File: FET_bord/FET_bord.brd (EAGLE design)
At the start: 100 x 80 mm, 4 parts

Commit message: スナバ回路資料追加
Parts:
- added CPOL1, CPOL2, CPOL3: C_DEKAI, user_rcl:1014CAPA
- added R1: 0, user_rcl:1608
- added R_I1, R_I2: (no value), user_rcl:0603X4RESISTOR
- added U$1: VL_4P, user_conector:VL_4P
- added U$2: A3921, user_ic:TSSOP_28P_ALLEGRO
- added U$3: ACS711, user_ic:SOIC8
- added U$4: HS38382, user_heatshink:38X38SQ
- added U$5, U$7: FDC6305, user_tr_fet_igbt:SSOT6
- added U$6: RGB_LED, user_leds:RGB_LED
- added U$8: TLP290-4, user_ic:TLP290
- moved TR2 81.3 mm to (47.0, 31.8), turned to 270 degrees
- moved TR1 66.1 mm to (47.0, 7.62), turned to 270 degrees
- moved TR4 53.3 mm to (21.6, 31.8), turned to 270 degrees
- moved TR3 47.3 mm to (21.6, 7.62), turned to 270 degrees
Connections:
- new net FF1: U$5.1, U$7.1
- new net FF2: U$5.3, U$7.3
- new net GHA: U$2.PIN10
- new net GHB: U$2.PIN5
- new net GLA: U$2.PIN12
- new net GLB: U$2.PIN3
- new net GND: CPOL1.-, CPOL2.-, CPOL3.-, R1.2, TR3.3, TR4.3, U$1.P$4
- new net GNDI: R1.1, U$2.PAD, U$2.PIN17, U$5.2, U$5.5, U$6.B_A
- new net M: U$1.P$3, U$3.P$1, U$3.P$2
- new net N$1: U$5.6, U$6.R_A
- new net N$2: TR1.3, TR3.2, U$3.P$3, U$3.P$4
- new net N$3: TR2.3, TR4.2
- new net N$4: U$1.P$2
- new net N$5: U$5.4, U$6.G_A
- new net N$6: R_I1.1, U$6.R_K
- new net N$7: R_I1.2, U$6.G_K
- new net N$8: R_I1.3, U$6.B_K
- new net SA: U$2.PIN11
- new net SB: U$2.PIN4
- new net VDD: CPOL1.+, CPOL2.+, CPOL3.+, TR1.2, TR2.2, U$1.P$1
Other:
- board size 100 x 80 mm -> 85 x 54 mm

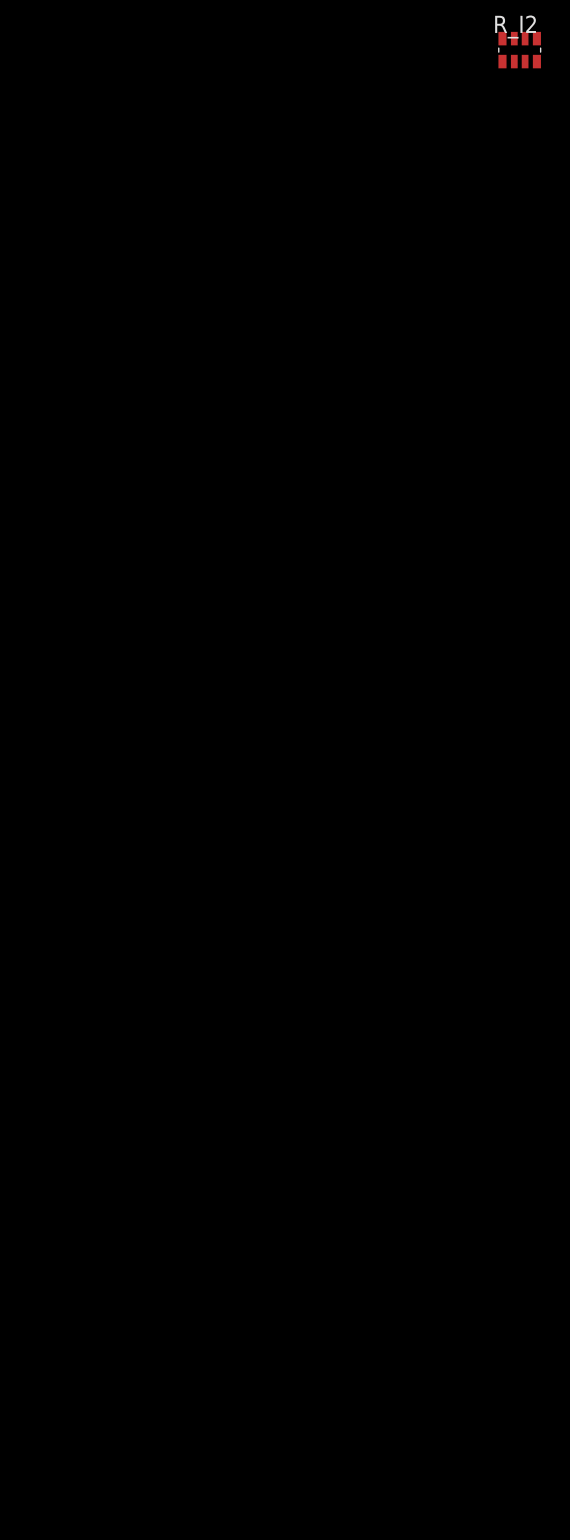
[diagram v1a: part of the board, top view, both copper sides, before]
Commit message: スナバ追加
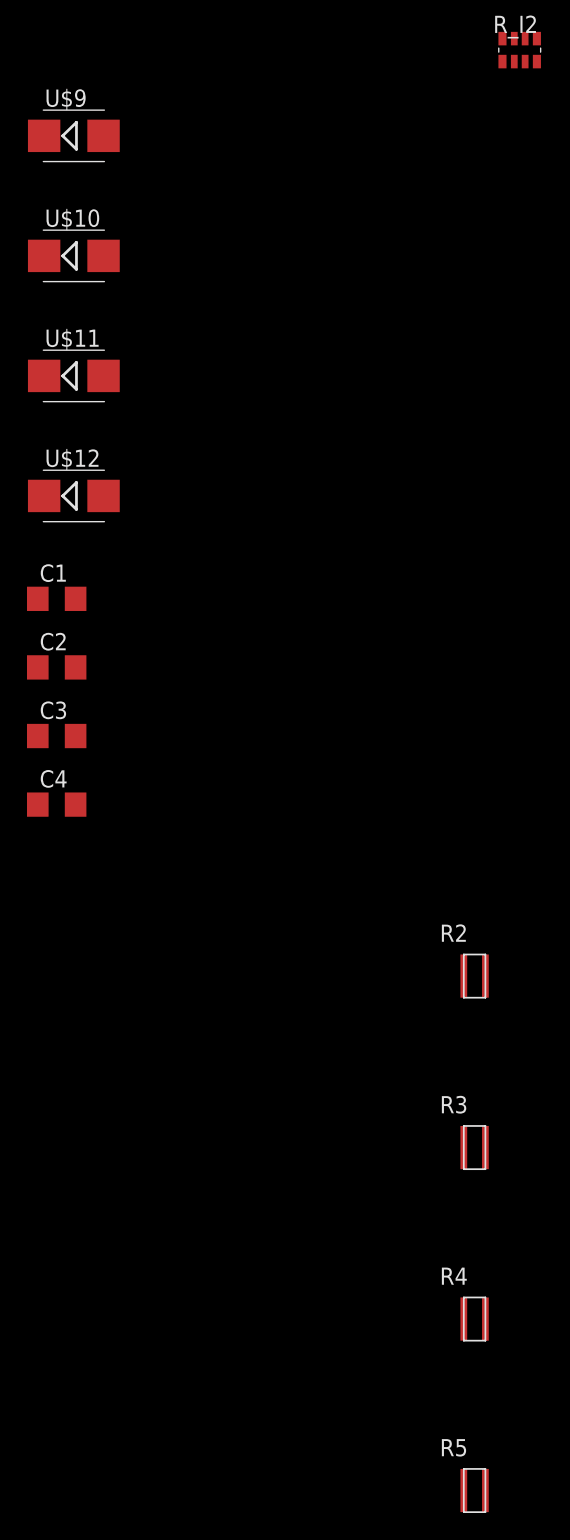
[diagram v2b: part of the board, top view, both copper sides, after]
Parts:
- added C1, C2, C3, C4: 0.1u, rcl:C3216
- added R2, R3, R4, R5: (no value), user_rcl:1632
- added U$10, U$11, U$12, U$9: ES3BB13F, user_diode:SMB
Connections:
- new net N$10: C2.2, R3.P$2, U$9.A
- new net N$11: C3.2, R4.P$2, U$12.A
- new net N$12: C4.1, R5.P$1, U$11.C
- new net N$9: C1.1, R2.P$1, U$10.C
- net GND: now also C1.2, C4.2, R3.P$1, R4.P$1
- net N$2: now also U$10.A, U$9.C
- net N$3: now also U$11.A, U$12.C
- net VDD: now also C2.1, C3.1, R2.P$2, R5.P$2

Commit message: a3921ロジック回路周りの設計
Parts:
- added C5: 0.1u, rcl:C1608
- added R6: (no value), user_rcl:1608
- added R7: 20k, user_rcl:1608
- added R_I3, R_I4: 10k, user_rcl:1005X4RESISTOR
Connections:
- new net N$13: R_I3.1, U$2.PIN23
- new net N$14: R_I3.2, U$2.PIN22
- new net N$15: R_I3.3, U$2.PIN21
- new net N$16: R_I3.4, U$2.PIN19
- new net RDEAD: U$2.PIN27
- new net RESET: U$2.PIN24
- new net V5: C5.1, R_I3.5, R_I3.6, R_I3.7, R_I4.5, R_I4.6, R_I4.7, U$2.PIN20
- new net VDSTH: R6.1, R7.1, R_I4.1, R_I4.4, U$2.PIN28
- net FF1: now also R_I4.2, U$2.PIN25
- net FF2: now also R_I4.3, U$2.PIN26
- net GNDI: now also C5.2, R6.2, R7.2, R_I3.8, R_I4.8
- net VDD: now also U$2.PIN13
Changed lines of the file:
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@@
 <attribute name="VALUE" x="-33.02" y="-105.41" size="1.27" layer="27"/>
+</element>
+<element name="R_I3" library="user_rcl" package="1005X4RESISTOR" value="10k" x="-33.02" y="-157.48" smashed="yes"/>
+<element name="R_I4" library="user_rcl" package="1005X4RESISTOR" value="10k" x="-33.02" y="-160.02" smashed="yes"/>
+<element name="C5" library="rcl" library_urn="urn:adsk.eagle:library:334" package="C1608" package3d_urn="urn:adsk.eagle:package:23621/2" value="0.1u" x="-31.75" y="-163.83" smashed="yes">
+<attribute name="NAME" x="-32.385" y="-163.195" size="1.27" layer="25"/>
+<attribute name="POPULARITY" value="3" x="-31.75" y="-163.83" size="1.778" layer="27" display="off"/>
+<attribute name="SPICEPREFIX" value="C" x="-31.75" y="-163.83" size="1.778" layer="27" display="off"/>
+<attribute name="VALUE" x="-32.385" y="-165.735" size="1.27" layer="27"/>
+</element>
+<element name="R6" library="user_rcl" package="1608" value="" x="-31.75" y="-168.91" smashed="yes">
+<attribute name="NAME" x="-32.385" y="-168.275" size="1.27" layer="25"/>
+<attribute name="VALUE" x="-32.385" y="-170.815" size="1.27" layer="27"/>
+</element>
+<element name="R7" library="user_rcl" package="1608" value="20k" x="-31.75" y="-172.72" smashed="yes">
+<attribute name="NAME" x="-32.385" y="-172.085" size="1.27" layer="25"/>
+<attribute name="VALUE" x="-32.385" y="-174.625" size="1.27" layer="27"/>
 </element>
 </elements>
@@
 <contactref element="R2" pad="P$2"/>
 <contactref element="R5" pad="P$2"/>
+<contactref element="U$2" pad="PIN13"/>
 <wire x1="0" y1="-115.57" x2="0" y2="-153.67" width="0" layer="19" extent="1-1"/>
 <wire x1="-33.15" y1="-97.79" x2="0" y2="-115.57" width="0" layer="19" extent="1-1"/>
@@
 <wire x1="45.72" y1="41.189" x2="34.29" y2="41.189" width="0" layer="19" extent="1-1"/>
 <wire x1="49.53" y1="31.75" x2="45.72" y2="41.189" width="0" layer="19" extent="1-1"/>
-<wire x1="49.53" y1="7.62" x2="49.53" y2="31.75" width="0" layer="19" extent="1-1"/>
+<wire x1="60.31" y1="15.68" x2="49.53" y2="31.75" width="0" layer="19" extent="1-1"/>
+<wire x1="49.53" y1="7.62" x2="60.31" y2="15.68" width="0" layer="19" extent="1-1"/>
 </signal>
 <signal name="N$3">
@@
 <contactref element="U$5" pad="5"/>
 <contactref element="U$5" pad="2"/>
-<wire x1="2.54" y1="-22.89" x2="76.36" y2="13.66" width="0" layer="19" extent="1-1"/>
+<contactref element="R_I3" pad="8"/>
+<contactref element="C5" pad="2"/>
+<contactref element="R6" pad="2"/>
+<contactref element="R7" pad="2"/>
+<contactref element="R_I4" pad="8"/>
+<wire x1="-30.9" y1="-168.91" x2="-30.9" y2="-172.72" width="0" layer="19" extent="1-1"/>
+<wire x1="-30.9" y1="-163.83" x2="-30.9" y2="-168.91" width="0" layer="19" extent="1-1"/>
+<wire x1="-32.82" y1="-159.72" x2="-30.9" y2="-163.83" width="0" layer="19" extent="1-1"/>
+<wire x1="-32.82" y1="-157.18" x2="-32.82" y2="-159.72" width="0" layer="19" extent="1-1"/>
+<wire x1="2.54" y1="-22.89" x2="-32.82" y2="-157.18" width="0" layer="19" extent="1-1"/>
 <wire x1="2.54" y1="-20.29" x2="2.54" y2="-22.89" width="0" layer="19" extent="1-1"/>
 <wire x1="1.69" y1="-15.24" x2="2.54" y2="-20.29" width="0" layer="19" extent="1-1"/>
 <wire x1="62.902" y1="19.224" x2="1.69" y2="-15.24" width="0" layer="19" extent="1-1"/>
 <wire x1="65.51" y1="16.33" x2="62.902" y2="19.224" width="0" layer="19" extent="1-1"/>
+<wire x1="76.36" y1="13.66" x2="65.51" y2="16.33" width="0" layer="19" extent="1-1"/>
 </signal>
 <signal name="GLB">
@@
 <contactref element="U$5" pad="3"/>
 <contactref element="U$7" pad="3"/>
+<contactref element="U$2" pad="PIN26"/>
+<contactref element="R_I4" pad="3"/>
+<wire x1="3.49" y1="-35.59" x2="-31.77" y2="-160.82" width="0" layer="19" extent="1-1"/>
 <wire x1="3.49" y1="-22.89" x2="3.49" y2="-35.59" width="0" layer="19" extent="1-1"/>
+<wire x1="65.51" y1="22.18" x2="3.49" y2="-22.89" width="0" layer="19" extent="1-1"/>
 </signal>
 <signal name="FF1">
 <contactref element="U$5" pad="1"/>
 <contactref element="U$7" pad="1"/>
+<contactref element="U$2" pad="PIN25"/>
+<contactref element="R_I4" pad="2"/>
+<wire x1="1.59" y1="-35.59" x2="-32.27" y2="-160.82" width="0" layer="19" extent="1-1"/>
 <wire x1="1.59" y1="-22.89" x2="1.59" y2="-35.59" width="0" layer="19" extent="1-1"/>
+<wire x1="65.51" y1="21.53" x2="1.59" y2="-22.89" width="0" layer="19" extent="1-1"/>
 </signal>
 <signal name="N$9">
@@
 <wire x1="-32.68" y1="-71.12" x2="-33.15" y2="-102.87" width="0" layer="19" extent="1-1"/>
 </signal>
+<signal name="N$13">
+<contactref element="U$2" pad="PIN23"/>
+<contactref element="R_I3" pad="1"/>
+<wire x1="65.51" y1="20.23" x2="-32.82" y2="-158.28" width="0" layer="19" extent="1-1"/>
+</signal>
+<signal name="N$14">
+<contactref element="U$2" pad="PIN22"/>
+<contactref element="R_I3" pad="2"/>
+<wire x1="65.51" y1="19.58" x2="-32.27" y2="-158.28" width="0" layer="19" extent="1-1"/>
+</signal>
+<signal name="N$15">
+<contactref element="U$2" pad="PIN21"/>
+<contactref element="R_I3" pad="3"/>
+<wire x1="65.51" y1="18.93" x2="-31.77" y2="-158.28" width="0" layer="19" extent="1-1"/>
+</signal>
+<signal name="N$16">
+<contactref element="U$2" pad="PIN19"/>
+<contactref element="R_I3" pad="4"/>
+<wire x1="65.51" y1="17.63" x2="-31.22" y2="-158.28" width="0" layer="19" extent="1-1"/>
+</signal>
+<signal name="V5">
+<contactref element="U$2" pad="PIN20"/>
+<contactref element="R_I3" pad="7"/>
+<contactref element="R_I3" pad="6"/>
+<contactref element="R_I3" pad="5"/>
+<contactref element="C5" pad="1"/>
+<contactref element="R_I4" pad="7"/>
+<contactref element="R_I4" pad="6"/>
+<contactref element="R_I4" pad="5"/>
+<wire x1="-32.27" y1="-159.72" x2="-32.6" y2="-163.83" width="0" layer="19" extent="1-1"/>
+<wire x1="-31.77" y1="-159.72" x2="-32.27" y2="-159.72" width="0" layer="19" extent="1-1"/>
+<wire x1="-31.22" y1="-159.72" x2="-31.77" y2="-159.72" width="0" layer="19" extent="1-1"/>
+<wire x1="-32.27" y1="-157.18" x2="-32.27" y2="-159.72" width="0" layer="19" extent="1-1"/>
+<wire x1="-31.77" y1="-157.18" x2="-32.27" y2="-157.18" width="0" layer="19" extent="1-1"/>
+<wire x1="-31.22" y1="-157.18" x2="-31.77" y2="-157.18" width="0" layer="19" extent="1-1"/>
+<wire x1="65.51" y1="18.28" x2="-31.22" y2="-157.18" width="0" layer="19" extent="1-1"/>
+</signal>
+<signal name="VDSTH">
+<contactref element="U$2" pad="PIN28"/>
+<contactref element="R_I4" pad="4"/>
+<contactref element="R6" pad="1"/>
+<contactref element="R7" pad="1"/>
+<contactref element="R_I4" pad="1"/>
+<wire x1="-32.6" y1="-168.91" x2="-32.6" y2="-172.72" width="0" layer="19" extent="1-1"/>
+<wire x1="-32.82" y1="-160.82" x2="-32.6" y2="-168.91" width="0" layer="19" extent="1-1"/>
+<wire x1="-31.22" y1="-160.82" x2="-32.82" y2="-160.82" width="0" layer="19" extent="1-1"/>
+<wire x1="65.51" y1="23.48" x2="-31.22" y2="-160.82" width="0" layer="19" extent="1-1"/>
+</signal>
+<signal name="RDEAD">
+<contactref element="U$2" pad="PIN27"/>
+</signal>
+<signal name="RESET">
+<contactref element="U$2" pad="PIN24"/>
+</signal>
 </signals>

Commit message: ロジック部を設計
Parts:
- removed U$8: TLP290-4, user_ic:TLP290
- added C6: 0.1u, rcl:C1608
- added IC_1: (no value), user_ic:TLP291
- added IC_2: (no value), user_ic:TLP290
- added IC_3: (no value), user_ic:SO6-5
- added R10, R9: 10k, user_rcl:1608
- added R8: 33k, user_rcl:1608
- added R_I5: 1k, user_rcl:0603X4RESISTOR
- R6: value (none) -> 2.4k
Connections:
- new net +3V3: R10.2, R9.2
- new net COAST: IC_2.2_C, R_I3.3, U$2.PIN21, U$2.PIN22
- new net COAST_IN: R_I5.4
- new net DIR: IC_2.1_C, R_I3.4, U$2.PIN19
- new net DIR_IN: R_I5.3
- new net FF1O: IC_2.3_K, R_I2.8
- new net FF1_IN: IC_2.3_C, R9.1
- new net FF2O: IC_2.4_K, R_I2.5
- new net FF2_IN: IC_2.4_C, R10.1
- new net GNDINT: IC_1.PIN2, IC_2.1_K, IC_2.2_K, IC_2.3_E, IC_2.4_E, IC_3.3
- new net N$17: IC_2.1_A, R_I5.6
- new net N$18: IC_2.2_A, R_I5.5
- new net PWM: IC_3.5, R_I3.1, U$2.PIN23
- new net PWM_IN: R_I5.1
- new net RESET_IN: R_I5.2
- net GNDI: now also C6.2, IC_1.PIN3, IC_2.1_E, IC_2.2_E, IC_3.4, U$7.2, U$7.5
- net N$13: now also IC_3.1, R_I5.8; no longer R_I3.1, U$2.PIN23
- net N$14: now also R_I2.4, U$7.4; no longer R_I3.2, U$2.PIN22
- net N$15: now also R_I2.1, U$7.6; no longer R_I3.3, U$2.PIN21
- net N$16: now also IC_1.PIN1, R_I5.7; no longer R_I3.4, U$2.PIN19
- net RDEAD: now also R7.1, R_I4.1
- net RESET: now also IC_1.PIN4, R8.1
- net V5: now also C6.1, IC_2.3_A, IC_2.4_A, IC_3.6, R8.2, R_I1.6, R_I1.7, R_I1.8; no longer R_I3.7
- net VDSTH: no longer R7.1, R_I4.1

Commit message: 回路図ほぼ完成
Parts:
- added C10: 10u, rcl:C1608
- added C11, C12, C13, C14: 0.1u, rcl:C1608
- added C15: 4.7u, rcl:C1608
- added C16, C19: 2.2u, rcl:C1608
- added C17: 100u, rcl:C3216
- added C18, C7: 1u, rcl:C1608
- added C8, C9: 0.22u, rcl:C1608
- added CON1, CON2: (no value), user_conector:JQ_P8P
- added IC1: (no value), user_ic:SOT23-5
- added IC2: (no value), user_ic:SOT23-6
- added L1: 22u, user_rcl:SMD_INDUCTOR
- added R11, R12, R13, R14, R15, R16, R17, R18, R19: (no value), user_rcl:1608
- added R20: 3.3k, user_rcl:1608
- added R21: 2k, user_rcl:1608
- added R22: 10k, user_rcl:1608
- added U$13: HS38382, user_heatshink:38X38SQ
- added U$8: BOX10PBOX10P-L, user_conector:BOX10P-L
- CPOL1, CPOL2, CPOL3: value C_DEKAI -> 330u
- U$4: value HS38382 -> ss2040; device user_heatshink:38X38SQ -> user_diode:SOD_123
- moved U$4 361.2 mm to (-30.5, -358.1)
- moved IC_2 244.8 mm to (61.0, 41.9)
- moved U$6 15.3 mm to (74.9, 25.4)
- moved U$2 8.98 mm to (62.2, 33.0)
- moved U$3 3.59 mm to (35.6, 15.2), flipped to the bottom, turned to 180 degrees
- moved TR1 1.27 mm to (47.0, 8.89), flipped to the bottom, turned to 90 degrees
- moved TR3 1.27 mm to (21.6, 8.89), flipped to the bottom, turned to 90 degrees
- flipped TR2 to the bottom, turned to 90 degrees
- flipped TR4 to the bottom, turned to 90 degrees
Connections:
- removed net N$3: TR2.3, TR4.2, U$11.A, U$12.C
- new net 12V: C19.1, IC2.5, R22.2, U$8.P$1, U$8.P$2
- new net 5V: C15.1, IC1.1, IC1.3, U$8.P$10, U$8.P$9
- new net CANH: U$8.P$5
- new net CANL: U$8.P$6
- new net FAULT: CON2.P$4, R19.1, U$3.P$6
- new net N$19: C7.1, U$2.PIN16
- new net N$20: C7.2, U$2.PIN15
- new net N$21: C8.2, U$2.PIN9
- new net N$22: C9.2, U$2.PIN6
- new net N$23: C10.2, U$2.PIN8
- new net N$24: C18.2, IC2.3, R20.1, R21.2
- new net N$25: R13.2, R17.2, TR4.1
- new net N$26: R14.2, R18.2, TR2.1
- new net N$27: R11.2, R15.2, TR1.1
- new net N$28: R12.2, R16.2, TR3.1
- new net N$31: IC2.4, R22.1
- new net SENS_GND: C14.1, U$3.P$5
- new net SENS_VCC: C14.2, C16.1, IC1.5, R19.2, U$3.P$8
- new net VIOUT: CON2.P$2, U$3.P$7
- net +3V3: now also C17.1, C18.1, L1.P$2, R20.2
- net GHA: now also R18.1
- net GHB: now also R15.1
- net GLA: now also R17.1
- net GLB: now also R16.1
- net GND: now also C11.2, C12.2, C13.2, R12.1, R13.1
- net GNDI: now also C10.1, U$2.PIN2
- net GNDINT: now also C15.2, C16.2, C17.2, C19.2, CON2.P$1, CON2.P$3, IC1.2, IC2.2, R21.1, U$4.A, U$8.P$7, U$8.P$8
- net N$2: now also IC2.6, L1.P$1, U$4.K; no longer TR1.3, TR3.2, U$10.A, U$3.P$3, U$3.P$4, U$9.C
- net SA: now also C8.1, R14.1, TR2.3, TR4.2, U$11.A, U$12.C
- net SB: now also C9.1, R11.1, TR1.3, TR3.2, U$10.A, U$3.P$3, U$3.P$4, U$9.C
- net VDD: now also C11.1, C12.1, C13.1, U$2.PIN1

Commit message: 基板設計を開始した
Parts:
- removed C1, C2, C3, C4: 0.1u, rcl:C3216
- removed R2, R3, R4, R5: (no value), user_rcl:1632
- R11, R12, R13, R14: value (none) -> 10k
- R15, R16, R17, R18: value (none) -> 10
- U$10, U$11, U$12, U$9: value ES3BB13F -> SBR15U30SP5; device user_diode:SMB -> user_diode:POWERDI_5
- moved U$4 410.6 mm to (72.4, 39.4), flipped to the bottom, turned to 270 degrees
- moved C19 399.7 mm to (76.2, 33.0), flipped to the bottom, turned to 180 degrees
- moved R22 395.3 mm to (73.7, 34.3), flipped to the bottom, turned to 180 degrees
- moved C18 393.4 mm to (80.0, 35.6), turned to 180 degrees
- moved R21 386.6 mm to (77.5, 34.3), turned to 90 degrees
- moved R20 386.1 mm to (80.0, 36.8), flipped to the bottom, turned to 180 degrees
- moved C17 383.2 mm to (82.5, 39.4), flipped to the bottom, turned to 270 degrees
- moved L1 374.5 mm to (73.7, 41.9)
- moved IC2 361.5 mm to (74.9, 35.6), turned to 180 degrees
- moved C16 324.2 mm to (63.5, 6.35), flipped to the bottom, turned to 270 degrees
- moved C15 321.7 mm to (71.1, 6.35), flipped to the bottom, turned to 270 degrees
- moved IC1 315.7 mm to (67.3, 6.35), flipped to the bottom, turned to 270 degrees
- moved C14 315.5 mm to (39.4, 20.3), flipped to the bottom, turned to 270 degrees
- moved R18 314.5 mm to (40.6, 26.7), flipped to the bottom
- moved R19 314.2 mm to (39.4, 22.9), flipped to the bottom, turned to 270 degrees
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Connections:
- removed net N$10: C2.2, R3.P$2, U$9.A
- removed net N$11: C3.2, R4.P$2, U$12.A
- removed net N$12: C4.1, R5.P$1, U$11.C
- removed net N$9: C1.1, R2.P$1, U$10.C
- net GND: now also U$10.1, U$10.2, U$11.1, U$11.2; no longer C1.2, C4.2, R3.P$1, R4.P$1
- net SA: now also U$11.3, U$12.1, U$12.2; no longer U$11.A, U$12.C
- net SB: now also U$10.3, U$9.1, U$9.2; no longer U$10.A, U$9.C
- net VDD: now also U$12.3, U$9.3; no longer C2.1, C3.1, R2.P$2, R5.P$2

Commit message: スナバ消した。基盤が結構仕上がってきた
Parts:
- removed R_I5: 1k, user_rcl:0603X4RESISTOR
- added C1: 0.1u, rcl:C1608
- added R2, R3, R4, R5: 1k, user_rcl:1608
- moved U$13 358.5 mm to (12.7, -44.5)
- moved IC_1 43.7 mm to (81.3, 6.35), turned to 90 degrees
- moved IC_3 35.0 mm to (79.1, 9.91), turned to 90 degrees
- moved C6 27.3 mm to (76.1, 12.2), turned to 270 degrees
- moved U$11 25.0 mm to (19.1, 13.6)
- moved U$12 24.6 mm to (41.9, 13.6)
- moved R18 24.3 mm to (38.1, 2.54)
- moved TR1 24.3 mm to (44.5, 33.0)
- moved TR2 24.3 mm to (44.5, 7.62)
- moved R13 24.2 mm to (11.4, 7.62)
- moved R14 24.2 mm to (34.3, 7.62)
- moved TR3 24.1 mm to (21.6, 33.0)
- moved TR4 24.1 mm to (21.6, 7.62)
- moved R17 22.9 mm to (15.2, 2.54)
- moved R11 20.4 mm to (34.3, 29.2)
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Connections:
- removed net CANH: U$8.P$5
- removed net CANL: U$8.P$6
- removed net N$14: R_I2.4, U$7.4
- removed net N$15: R_I2.1, U$7.6
- removed net N$4: U$1.P$2
- removed net SENS_GND: C14.1, U$3.P$5
- new net CAN_N: CON2.P$8, U$8.P$6
- new net CAN_P: CON2.P$7, U$8.P$5
- new net N$3: R_I2.1, U$7.4
- new net N$9: R_I2.4, U$7.6
- net +3V3: now also CON1.P$5, CON1.P$6
- net COAST_IN: now also CON1.P$3, R5.1; no longer R_I5.4
- net DIR_IN: now also CON1.P$4, R4.1; no longer R_I5.3
- net FF1: now also R_I4.3; no longer R_I4.2
- net FF1O: now also R_I2.5; no longer R_I2.8
- net FF1_IN: now also CON1.P$2
- net FF2: now also R_I4.2; no longer R_I4.3
- net FF2O: now also R_I2.8; no longer R_I2.5
- net FF2_IN: now also CON1.P$1
- net GND: now also U$1.P$1, U$2.PIN2; no longer U$1.P$4
- net GNDI: now also C1.2, U$6.B_K; no longer U$2.PIN2, U$6.B_A
- net GNDINT: now also C14.1, CON1.P$7, CON1.P$8, U$3.P$5
- net M: now also U$1.P$2, U$3.P$3, U$3.P$4; no longer U$1.P$3, U$3.P$1, U$3.P$2
- net N$1: now also U$6.G_K; no longer U$6.R_A
- net N$13: now also R2.2; no longer R_I5.8
- net N$16: now also R3.2; no longer R_I5.7
- net N$17: now also R4.2; no longer R_I5.6
- net N$18: now also R5.2; no longer R_I5.5
- net N$5: now also U$6.R_K; no longer U$6.G_A
- net N$6: now also U$6.B_A; no longer U$6.R_K
- net N$7: now also U$6.G_A; no longer U$6.G_K
- net N$8: now also U$6.R_A; no longer U$6.B_K
- net PWM_IN: now also CON2.P$5, R2.1; no longer R_I5.1
- net RESET_IN: now also CON2.P$6, R3.1; no longer R_I5.2
- net SA: now also U$3.P$1, U$3.P$2
- net SB: now also U$1.P$3; no longer U$3.P$3, U$3.P$4
- net VDD: now also C1.1, U$1.P$4; no longer U$1.P$1
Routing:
- net GNDINT: track 0.00 -> 250.6 mm, vias 0 -> 8
- net GND: track 0.00 -> 167.8 mm, vias 0 -> 3
- net VDD: track 0.00 -> 96.0 mm, vias 0 -> 1
- net +3V3: track 0.00 -> 73.9 mm, vias 0 -> 5
- net V5: track 0.00 -> 72.3 mm, vias 0 -> 7
- net GLA: track 0.00 -> 58.3 mm, vias 0 -> 1
- net FAULT: track 0.00 -> 52.4 mm, vias 0 -> 1
- net SA: track 0.00 -> 52.4 mm, vias 0 -> 1
- net SENS_VCC: track 0.00 -> 50.8 mm, vias 0 -> 2
- net VIOUT: track 0.00 -> 42.1 mm, vias 0 -> 1
- net CAN_P: track 0.00 -> 37.2 mm, vias 0 -> 1
- net 5V: track 0.00 -> 36.7 mm
- net GHA: track 0.00 -> 36.0 mm, vias 0 -> 1
- net CAN_N: track 0.00 -> 35.4 mm, vias 0 -> 1
- net DIR: track 0.00 -> 34.7 mm, vias 0 -> 4
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- added copper zone on layer 1, net +3V3
- added copper zone on layer 16, net +3V3
- added copper zone on layer 1, net GNDI
- added copper zone on layer 16, net GNDI
- added copper zone on layer 1, net GNDINT
- added copper zone on layer 16, net GNDINT
- added copper zone on layer 16, net N$2
- added copper zone on layer 16, net V5
- added copper zone on layer 16, net VCC
